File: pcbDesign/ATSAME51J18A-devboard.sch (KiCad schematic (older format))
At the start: 36 parts

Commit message: Finished schematic v0.1
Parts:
- removed C?: 0.47u, Capacitor_SMD:C_0402_1005Metric, symbol Device:C
- removed C? (x2): C, Capacitor_SMD:C_0402_1005Metric, symbol Device:C
- removed C? (x2): 4.7u, Capacitor_SMD:C_0402_1005Metric, symbol Device:C
- removed D?: APA102-2020, LED_SMD:LED-APA102-2020, symbol LED:APA102-2020
- removed D? (x5): D_Schottky, symbol Device:D_Schottky
- removed R?: 10K, Resistor_SMD:R_0402_1005Metric, symbol Device:R
- removed R? (x2): 5.1k, Resistor_SMD:R_0402_1005Metric, symbol Device:R_Small
- removed R?: 0.01, Resistor_SMD:R_0402_1005Metric, symbol Device:R_Small
- removed R? (x2): 10k, Resistor_SMD:R_0402_1005Metric, symbol Device:R_Small
- removed R?: 1k, Resistor_SMD:R_0402_1005Metric, symbol Device:R_Small
- removed R?: 2k, Resistor_SMD:R_0402_1005Metric, symbol Device:R_Small
- removed R?: 1.18k, Resistor_SMD:R_0402_1005Metric, symbol Device:R_Small
- removed R?: 1.13k, Resistor_SMD:R_0402_1005Metric, symbol Device:R_Small
- removed R?: 46.4k, Resistor_SMD:R_0402_1005Metric, symbol Device:R_Small
- removed U?: ATSAME51J18A-A, Package_QFP:TQFP-64_10x10mm_P0.5mm, symbol MCU_Microchip_SAME:ATSAME51J18A-A
- removed U?: LM27762, Package_SON:WSON-12-1EP_3x2mm_P0.5mm_EP1x2.65_ThermalVias, symbol Regulator_SwitchedCapacitor:LM27762
- removed U?: BQ24074RGT, Package_DFN_QFN:VQFN-16-1EP_3x3mm_P0.5mm_EP1.6x1.6mm, symbol Battery_Management:BQ24074RGT
- removed U?: BQ27441DRZR-G1B, Package_SON:Texas_S-PDSO-N12, symbol Battery_Management:BQ27441DRZR-G1B
- removed U?: LM2775QDSGTQ1, DSG0008A, symbol ATSAME51J18A-devboard-rescue:LM2775QDSGTQ1-2021-03-01_13-50-06
- removed U?: SC630AULTRT, SON_ULTRT_SEM, symbol ATSAME51J18A-devboard-rescue:SC630AULTRT-2021-03-02_13-26-31
- removed U?: MIC5219-5.0YMM, Package_SO:MSOP-8_3x3mm_P0.65mm, symbol Regulator_Linear:MIC5219-5.0YMM
- added D?: WS2812B, LED_SMD:LED_WS2812B_PLCC4_5.0x5.0mm_P3.2mm, symbol LED:WS2812B
- added J?: Conn_01x06_Male, symbol Connector:Conn_01x06_Male
- added J?: Conn_01x02_Male, symbol Connector:Conn_01x02_Male
- added J?: Conn_01x01_Male, symbol Connector:Conn_01x01_Male
- added R? (x2): 5.1k, Resistor_SMD:R_0402_1005Metric, symbol Device:R_Small
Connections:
- net labels added: CAN_RX, CAN_S, CAN_TX, NEOPIXEL_DIN, NEOPIXEL_DOUT, QCS, QDAT0, QDAT1, QDAT2, QDAT3, QSCK
- net labels removed: 10[IAT], 11[IPAT][Tx1], 12[IPAT][Rx1], 13[IPAT], 14[IADP], 15[IATP][SDCD], 16[IATP][SDWP], 17[IATP][SDA][QSPID0][SDCMD][I2SMCK], 18[IATP][SCL][QSPID1][SDDAT0][I2SFS], 19[IATP][QSPID2][SDDAT1][I2SSDO], 20[IATP][QSPID3][SDDAT2][I2SSDI], 23[IP][QSPISCK][SDDAT3][I2SSDI], 3[IAD], 4[IPAT][Vref], 5[IAT], 64[IPAT], 6[IAT], 9[IAT], CHARGE_ENABLE, CHARGE_MODE_CH0, CHARGE_MODE_CH1, USB_DETECT, VBUS_BAT_NREG, VBUS_NREG, VBUS_VIN_5V_REG, [SWCLK], [SWDIO]
- wire segments 75 -> 7
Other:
- moved on the sheet: J?, U?

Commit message: Cerrected errors in the schematic and began work on the pcb layout
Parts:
- removed P?: USB_C_Plug, symbol Connector:USB_C_Plug
- removed R?: 5.1k, Resistor_SMD:R_0402_1005Metric, symbol Device:R_Small
- added C1, C2: 100n, Capacitor_SMD:C_0402_1005Metric, symbol Device:C
- added D7: LED, LED_SMD:LED_0402_1005Metric, symbol Device:LED
- added J9: 12401598E4-2A, usb_c:12401598E4-2A, symbol usb_c:12401598E4-2A
- added R1: 5.1k, Resistor_SMD:R_0402_1005Metric, symbol Device:R_Small
- added R19: 10k, Resistor_SMD:R_0402_1005Metric, symbol Device:R_Small
- J1: renamed from J?; footprint (none) -> Connector_Card:microSD_HC_Hirose_DM3D-SF
- J2: renamed from J?; footprint JST_S2B-ZR-SM4A-TF(LF)(SN) -> S2B-ZR-SM4A-TF_LF__SN_:JST_S2B-ZR-SM4A-TF(LF)(SN)
- J3: renamed from J?; footprint JST_SM04B-SRSS-TB(LF)(SN) -> SM04B-SRSS-TB_LF__SN_:JST_SM04B-SRSS-TB(LF)(SN)
- J4, J8: renamed from J?; footprint (none) -> Connector_PinHeader_1.27mm:PinHeader_1x25_P1.27mm_Vertical
- J5: renamed from J?; footprint (none) -> Connector_PinHeader_1.27mm:PinHeader_1x01_P1.27mm_Vertical
- J6: renamed from J?; footprint (none) -> Connector_PinHeader_1.27mm:PinHeader_1x02_P1.27mm_Vertical
- J7: renamed from J?; footprint (none) -> Connector_PinHeader_1.27mm:PinHeader_1x06_P1.27mm_Vertical
- U1: renamed from U?; footprint D8_TEX -> ul_TCAN1051GVDRQ1:TCAN1051GVDRQ1
- gave numbers to parts that had none: 2
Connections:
- net labels added: LED_PIN
- wire segments 7 -> 3
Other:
- moved on the sheet: R2

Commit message: Fixed power rail enabling systems and rearanged pins for easier use
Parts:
- removed J4, J8: Conn_01x25, Connector_PinHeader_1.27mm:PinHeader_1x25_P1.27mm_Vertical, symbol Connector_Generic:Conn_01x25
- added J4: L_PINS, Connector_PinHeader_1.27mm:PinHeader_1x26_P1.27mm_Vertical, symbol Connector_Generic:Conn_01x26
- added J8: R_PINS, Connector_PinHeader_1.27mm:PinHeader_1x26_P1.27mm_Vertical, symbol Connector_Generic:Conn_01x26
- J2: value S2B-ZR-SM4A-TF(LF)(SN) -> BAT
- J3: value SM04B-SRSS-TB(LF)(SN) -> QWIIC
- J5: value Conn_01x01_Male -> NP_OUT
- J6: value Conn_01x02_Male -> USB
- J7: value Conn_01x06_Male -> QSPI
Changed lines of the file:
@@
 P 9300 3150
 F 0 "J3" H 9243 2583 50  0000 C CNN
-F 1 "SM04B-SRSS-TB(LF)(SN)" H 9243 2674 50  0000 C CNN
+F 1 "QWIIC" H 9243 2674 50  0000 C CNN
 F 2 "SM04B-SRSS-TB_LF__SN_:JST_SM04B-SRSS-TB(LF)(SN)" H 9300 3150 50  0001 L BNN
 F 3 "" H 9300 3150 50  0001 L BNN
@@
 P 9300 2350
 F 0 "J2" H 9192 1985 50  0000 C CNN
-F 1 "S2B-ZR-SM4A-TF(LF)(SN)" H 9192 2076 50  0000 C CNN
+F 1 "BAT" H 9192 2076 50  0000 C CNN
 F 2 "S2B-ZR-SM4A-TF_LF__SN_:JST_S2B-ZR-SM4A-TF(LF)(SN)" H 9300 2350 50  0001 L BNN
 F 3 "" H 9300 2350 50  0001 L BNN
@@
 Text GLabel 9250 4400 0    50   BiDi ~ 0
 VBUS_-3V3_CH2_REG
-$Comp
-L Connector_Generic:Conn_01x25 J8
-U 1 1 6061C495
-P 10650 5100
-F 0 "J8" H 10730 5142 50  0000 L CNN
-F 1 "Conn_01x25" H 10730 5051 50  0000 L CNN
-F 2 "Connector_PinHeader_1.27mm:PinHeader_1x25_P1.27mm_Vertical" H 10650 5100 50  0001 C CNN
-F 3 "~" H 10650 5100 50  0001 C CNN
-	1    10650 5100
-	1    0    0    -1
-$EndComp
 Text GLabel 10450 6300 0    50   BiDi ~ 0
 VBUS_-3V3_CH2_REG
@@
 Text GLabel 10450 4000 0    50   BiDi ~ 0
 VBUS_VIN_NREG
-Text GLabel 10450 3900 0    50   BiDi ~ 0
+Text GLabel 10450 3800 0    50   BiDi ~ 0
 VBUS_BAT
 Text GLabel 9250 4100 0    50   BiDi ~ 0
@@
 Text GLabel 10450 4100 0    50   BiDi ~ 0
 AREF
-$Comp
-L Connector_Generic:Conn_01x25 J4
-U 1 1 6045ED31
-P 9450 5100
-F 0 "J4" H 9530 5142 50  0000 L CNN
-F 1 "Conn_01x25" H 9530 5051 50  0000 L CNN
-F 2 "Connector_PinHeader_1.27mm:PinHeader_1x25_P1.27mm_Vertical" H 9450 5100 50  0001 C CNN
-F 3 "~" H 9450 5100 50  0001 C CNN
-	1    9450 5100
-	1    0    0    -1
-$EndComp
 Text GLabel 9250 6000 0    50   BiDi ~ 0
 31[Tx1]
@@
 Text GLabel 9250 4000 0    50   BiDi ~ 0
 RST
-Text GLabel 9250 3900 0    50   BiDi ~ 0
+Text GLabel 9250 3800 0    50   BiDi ~ 0
 EN
 Text GLabel 6550 5000 2    50   BiDi ~ 0
@@
 AR Path="/604C67EC" Ref="J7"  Part="1"
 F 0 "J7" H 10758 3731 50  0000 C CNN
-F 1 "Conn_01x06_Male" H 10758 3640 50  0000 C CNN
+F 1 "QSPI" H 10758 3640 50  0000 C CNN
 F 2 "Connector_PinHeader_1.27mm:PinHeader_1x06_P1.27mm_Vertical" H 10650 3350 50  0001 C CNN
 F 3 "~" H 10650 3350 50  0001 C CNN
@@
 P 10650 2700
 F 0 "J6" H 10758 2881 50  0000 C CNN
-F 1 "Conn_01x02_Male" H 10758 2790 50  0000 C CNN
+F 1 "USB" H 10758 2790 50  0000 C CNN
 F 2 "Connector_PinHeader_1.27mm:PinHeader_1x02_P1.27mm_Vertical" H 10650 2700 50  0001 C CNN
 F 3 "~" H 10650 2700 50  0001 C CNN
@@
 P 10650 2250
 F 0 "J5" H 10758 2431 50  0000 C CNN
-F 1 "Conn_01x01_Male" H 10758 2340 50  0000 C CNN
+F 1 "NP_OUT" H 10758 2340 50  0000 C CNN
 F 2 "Connector_PinHeader_1.27mm:PinHeader_1x01_P1.27mm_Vertical" H 10650 2250 50  0001 C CNN
 F 3 "~" H 10650 2250 50  0001 C CNN
@@
 	0    1    1    0
 $EndComp
+$Comp
+L Connector_Generic:Conn_01x26 J4
+U 1 1 60481B78
+P 9450 5000
+F 0 "J4" H 9530 4992 50  0000 L CNN
+F 1 "L_PINS" H 9530 4901 50  0000 L CNN
+F 2 "Connector_PinHeader_1.27mm:PinHeader_1x26_P1.27mm_Vertical" H 9450 5000 50  0001 C CNN
+F 3 "~" H 9450 5000 50  0001 C CNN
+	1    9450 5000
+	1    0    0    -1
+$EndComp
+$Comp
+L Connector_Generic:Conn_01x26 J8
+U 1 1 60485161
+P 10650 5000
+F 0 "J8" H 10730 4992 50  0000 L CNN
+F 1 "R_PINS" H 10730 4901 50  0000 L CNN
+F 2 "Connector_PinHeader_1.27mm:PinHeader_1x26_P1.27mm_Vertical" H 10650 5000 50  0001 C CNN
+F 3 "~" H 10650 5000 50  0001 C CNN
+	1    10650 5000
+	1    0    0    -1
+$EndComp
+$Comp
+L power:GND #PWR032
+U 1 1 60486DD1
+P 10450 3900
+F 0 "#PWR032" H 10450 3650 50  0001 C CNN
+F 1 "GND" V 10455 3772 50  0000 R CNN
+F 2 "" H 10450 3900 50  0001 C CNN
+F 3 "" H 10450 3900 50  0001 C CNN
+	1    10450 3900
+	0    1    1    0
+$EndComp
+$Comp
+L power:GND #PWR01
+U 1 1 60489437
+P 9250 3900
+F 0 "#PWR01" H 9250 3650 50  0001 C CNN
+F 1 "GND" V 9255 3772 50  0000 R CNN
+F 2 "" H 9250 3900 50  0001 C CNN
+F 3 "" H 9250 3900 50  0001 C CNN
+	1    9250 3900
+	0    1    1    0
+$EndComp

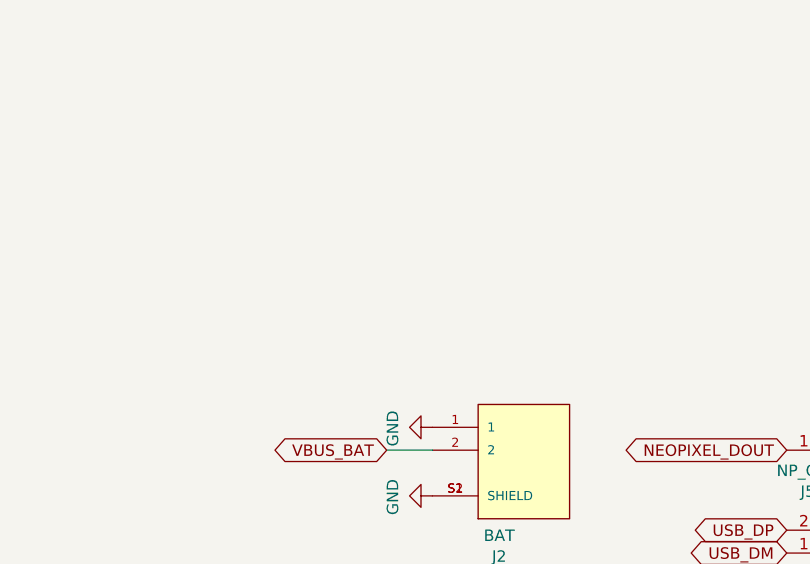
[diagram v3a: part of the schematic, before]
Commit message: Changed pin pitch to 2.54mm
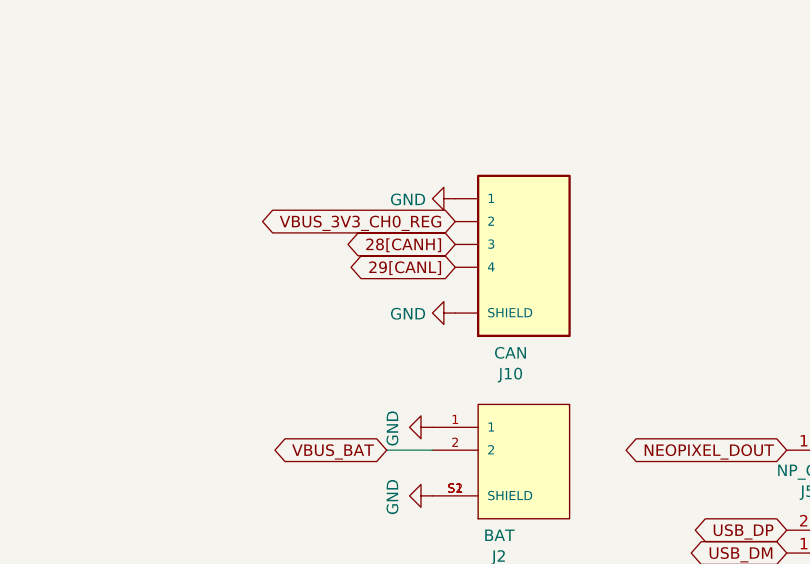
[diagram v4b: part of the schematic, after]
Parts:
- added J10: CAN, SM04B-SRSS-TB_LF__SN_:JST_SM04B-SRSS-TB(LF)(SN), symbol SM04B-SRSS-TB_LF__SN_:SM04B-SRSS-TB(LF)(SN)
- J4, J8: footprint Connector_PinHeader_1.27mm:PinHeader_1x26_P1.27mm_Vertical -> Connector_PinSocket_2.54mm:PinSocket_1x26_P2.54mm_Vertical
- J5: footprint Connector_PinHeader_1.27mm:PinHeader_1x01_P1.27mm_Vertical -> Connector_PinSocket_2.54mm:PinSocket_1x01_P2.54mm_Vertical
- J6: footprint Connector_PinHeader_1.27mm:PinHeader_1x02_P1.27mm_Vertical -> Connector_PinSocket_2.54mm:PinSocket_1x02_P2.54mm_Vertical
- J7: footprint Connector_PinHeader_1.27mm:PinHeader_1x06_P1.27mm_Vertical -> Connector_PinSocket_2.54mm:PinSocket_1x06_P2.54mm_Vertical
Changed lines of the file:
@@
 F 0 "J7" H 10758 3731 50  0000 C CNN
 F 1 "QSPI" H 10758 3640 50  0000 C CNN
-F 2 "Connector_PinHeader_1.27mm:PinHeader_1x06_P1.27mm_Vertical" H 10650 3350 50  0001 C CNN
+F 2 "Connector_PinSocket_2.54mm:PinSocket_1x06_P2.54mm_Vertical" H 10650 3350 50  0001 C CNN
 F 3 "~" H 10650 3350 50  0001 C CNN
 	1    10650 3350
@@
 F 0 "J6" H 10758 2881 50  0000 C CNN
 F 1 "USB" H 10758 2790 50  0000 C CNN
-F 2 "Connector_PinHeader_1.27mm:PinHeader_1x02_P1.27mm_Vertical" H 10650 2700 50  0001 C CNN
+F 2 "Connector_PinSocket_2.54mm:PinSocket_1x02_P2.54mm_Vertical" H 10650 2700 50  0001 C CNN
 F 3 "~" H 10650 2700 50  0001 C CNN
 	1    10650 2700
@@
 F 0 "J5" H 10758 2431 50  0000 C CNN
 F 1 "NP_OUT" H 10758 2340 50  0000 C CNN
-F 2 "Connector_PinHeader_1.27mm:PinHeader_1x01_P1.27mm_Vertical" H 10650 2250 50  0001 C CNN
+F 2 "Connector_PinSocket_2.54mm:PinSocket_1x01_P2.54mm_Vertical" H 10650 2250 50  0001 C CNN
 F 3 "~" H 10650 2250 50  0001 C CNN
 	1    10650 2250
@@
 F 0 "J4" H 9530 4992 50  0000 L CNN
 F 1 "L_PINS" H 9530 4901 50  0000 L CNN
-F 2 "Connector_PinHeader_1.27mm:PinHeader_1x26_P1.27mm_Vertical" H 9450 5000 50  0001 C CNN
+F 2 "Connector_PinSocket_2.54mm:PinSocket_1x26_P2.54mm_Vertical" H 9450 5000 50  0001 C CNN
 F 3 "~" H 9450 5000 50  0001 C CNN
 	1    9450 5000
@@
 F 0 "J8" H 10730 4992 50  0000 L CNN
 F 1 "R_PINS" H 10730 4901 50  0000 L CNN
-F 2 "Connector_PinHeader_1.27mm:PinHeader_1x26_P1.27mm_Vertical" H 10650 5000 50  0001 C CNN
+F 2 "Connector_PinSocket_2.54mm:PinSocket_1x26_P2.54mm_Vertical" H 10650 5000 50  0001 C CNN
 F 3 "~" H 10650 5000 50  0001 C CNN
 	1    10650 5000
@@
 	0    1    1    0
 $EndComp
+$Comp
+L SM04B-SRSS-TB_LF__SN_:SM04B-SRSS-TB(LF)(SN) J10
+U 1 1 604466EE
+P 9300 1350
+F 0 "J10" H 9243 783 50  0000 C CNN
+F 1 "CAN" H 9243 874 50  0000 C CNN
+F 2 "SM04B-SRSS-TB_LF__SN_:JST_SM04B-SRSS-TB(LF)(SN)" H 9300 1350 50  0001 L BNN
+F 3 "" H 9300 1350 50  0001 L BNN
+F 4 "JST" H 9300 1350 50  0001 L BNN "MANUFACTURER"
+F 5 "Manufacturer recommendations" H 9300 1350 50  0001 L BNN "STANDARD"
+	1    9300 1350
+	1    0    0    -1
+$EndComp
+$Comp
+L power:GND #PWR0116
+U 1 1 6044779D
+P 9000 1150
+F 0 "#PWR0116" H 9000 900 50  0001 C CNN
+F 1 "GND" V 9005 1022 50  0000 R CNN
+F 2 "" H 9000 1150 50  0001 C CNN
+F 3 "" H 9000 1150 50  0001 C CNN
+	1    9000 1150
+	0    1    1    0
+$EndComp
+Text GLabel 9000 1250 0    50   BiDi ~ 0
+VBUS_3V3_CH0_REG
+Text GLabel 9000 1350 0    50   BiDi ~ 0
+28[CANH]
+Text GLabel 9000 1450 0    50   BiDi ~ 0
+29[CANL]
+$Comp
+L power:GND #PWR0120
+U 1 1 604483DE
+P 9000 1650
+F 0 "#PWR0120" H 9000 1400 50  0001 C CNN
+F 1 "GND" V 9005 1522 50  0000 R CNN
+F 2 "" H 9000 1650 50  0001 C CNN
+F 3 "" H 9000 1650 50  0001 C CNN
+	1    9000 1650
+	0    1    1    0
+$EndComp

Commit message: Finnished routing
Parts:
- removed J9: 12401598E4-2A, usb_c:12401598E4-2A, symbol usb_c:12401598E4-2A
- added D8: PWR, LED_SMD:LED_0402_1005Metric, symbol Device:LED
- added D9: CHRG, LED_SMD:LED_0402_1005Metric, symbol Device:LED
- added J9: USB4105_REVA, USB4105_REVA:GCT_USB4105_REVA, symbol USB4105_REVA:USB4105_REVA
- added R23, R24: 10k, Resistor_SMD:R_0402_1005Metric, symbol Device:R_Small
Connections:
- net labels added: 30, 31, USB_N, USB_P
- net labels removed: 30[Rx1], 31[Tx1], USB_DM, USB_DP
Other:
- moved on the sheet: R1, R2
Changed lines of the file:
@@
 Comment4 ""
 $EndDescr
-Text GLabel 3800 1850 2    50   BiDi ~ 0
-USB_DP
+Text GLabel 4800 1300 0    50   BiDi ~ 0
+USB_P
 $Comp
 L power:GND #PWR0102
@@
 AREF
 Text GLabel 9250 6000 0    50   BiDi ~ 0
-31[Tx1]
+31
 Text GLabel 9250 5900 0    50   BiDi ~ 0
-30[Rx1]
+30
 Text GLabel 10450 6000 0    50   BiDi ~ 0
 29[CANL]
@@
 $EndComp
 Text GLabel 10450 2700 0    50   BiDi ~ 0
-USB_DM
+USB_N
 Text GLabel 10450 2600 0    50   BiDi ~ 0
-USB_DP
+USB_P
 $Sheet
 S 1950 2550 1150 900
@@
 L Device:R_Small R2
 U 1 1 6060BD83
-P 3900 1950
-F 0 "R2" H 3959 1996 50  0000 L CNN
-F 1 "5.1k" H 3959 1905 50  0000 L CNN
-F 2 "Resistor_SMD:R_0402_1005Metric" H 3900 1950 50  0001 C CNN
-F 3 "~" H 3900 1950 50  0001 C CNN
-	1    3900 1950
+P 6500 1200
+F 0 "R2" H 6559 1246 50  0000 L CNN
+F 1 "5.1k" H 6559 1155 50  0000 L CNN
+F 2 "Resistor_SMD:R_0402_1005Metric" H 6500 1200 50  0001 C CNN
+F 3 "~" H 6500 1200 50  0001 C CNN
+	1    6500 1200
 	0    -1   -1   0
 $EndComp
@@
 LED_PIN
 $Comp
-L Device:LED D7
-U 1 1 60430A33
-P 3150 6600
-F 0 "D7" V 3189 6482 50  0000 R CNN
-F 1 "LED" V 3098 6482 50  0000 R CNN
-F 2 "LED_SMD:LED_0402_1005Metric" H 3150 6600 50  0001 C CNN
-F 3 "~" H 3150 6600 50  0001 C CNN
-	1    3150 6600
-	0    -1   -1   0
-$EndComp
-$Comp
 L power:GND #PWR0101
 U 1 1 604318CC
@@
 	1    0    0    -1
 $EndComp
-$Comp
-L usb_c:12401598E4-2A J9
-U 1 1 604586E0
-P 2200 950
-F 0 "J9" H 3000 1337 60  0000 C CNN
-F 1 "12401598E4-2A" H 3000 1231 60  0000 C CNN
-F 2 "usb_c:12401598E4-2A" H 3000 1190 60  0001 C CNN
-F 3 "" H 2200 950 60  0000 C CNN
-	1    2200 950
-	1    0    0    -1
-$EndComp
-Text GLabel 3800 1550 2    50   BiDi ~ 0
+Text GLabel 6400 1000 2    50   BiDi ~ 0
 VBUS_USB_NREG
 Text GLabel 2200 1750 0    50   BiDi ~ 0
@@
 L power:GND #PWR0103
 U 1 1 6045FB57
-P 4000 1950
-F 0 "#PWR0103" H 4000 1700 50  0001 C CNN
-F 1 "GND" V 4005 1822 50  0000 R CNN
-F 2 "" H 4000 1950 50  0001 C CNN
-F 3 "" H 4000 1950 50  0001 C CNN
-	1    4000 1950
+P 6600 1200
+F 0 "#PWR0103" H 6600 950 50  0001 C CNN
+F 1 "GND" V 6605 1072 50  0000 R CNN
+F 2 "" H 6600 1200 50  0001 C CNN
+F 3 "" H 6600 1200 50  0001 C CNN
+	1    6600 1200
 	0    -1   -1   0
 $EndComp
@@
 L Device:R_Small R1
 U 1 1 60460985
-P 2100 1350
-F 0 "R1" H 2159 1396 50  0000 L CNN
-F 1 "5.1k" H 2159 1305 50  0000 L CNN
-F 2 "Resistor_SMD:R_0402_1005Metric" H 2100 1350 50  0001 C CNN
-F 3 "~" H 2100 1350 50  0001 C CNN
-	1    2100 1350
-	0    1    1    0
+P 4700 1200
+F 0 "R1" H 4759 1246 50  0000 L CNN
+F 1 "5.1k" H 4759 1155 50  0000 L CNN
+F 2 "Resistor_SMD:R_0402_1005Metric" H 4700 1200 50  0001 C CNN
+F 3 "~" H 4700 1200 50  0001 C CNN
+	1    4700 1200
+	0    -1   -1   0
 $EndComp
 $Comp
 L power:GND #PWR0105
 U 1 1 604625F2
-P 2000 1350
-F 0 "#PWR0105" H 2000 1100 50  0001 C CNN
-F 1 "GND" V 2005 1222 50  0000 R CNN
-F 2 "" H 2000 1350 50  0001 C CNN
-F 3 "" H 2000 1350 50  0001 C CNN
-	1    2000 1350
-	0    1    1    0
-$EndComp
-Text GLabel 2200 1450 0    50   BiDi ~ 0
-USB_DP
-Text GLabel 3800 1750 2    50   BiDi ~ 0
-USB_DM
-Text GLabel 2200 1550 0    50   BiDi ~ 0
-USB_DM
+P 4600 1200
+F 0 "#PWR0105" H 4600 950 50  0001 C CNN
+F 1 "GND" V 4605 1072 50  0000 R CNN
+F 2 "" H 4600 1200 50  0001 C CNN
+F 3 "" H 4600 1200 50  0001 C CNN
+	1    4600 1200
+	0    1    1    0
+$EndComp
+Text GLabel 6400 1300 2    50   BiDi ~ 0
+USB_P
+Text GLabel 4800 1400 0    50   BiDi ~ 0
+USB_N
+Text GLabel 6400 1400 2    50   BiDi ~ 0
+USB_N
 $Comp
 L power:GND #PWR0106
 U 1 1 60463C59
-P 3800 1250
-F 0 "#PWR0106" H 3800 1000 50  0001 C CNN
-F 1 "GND" V 3805 1122 50  0000 R CNN
-F 2 "" H 3800 1250 50  0001 C CNN
-F 3 "" H 3800 1250 50  0001 C CNN
-	1    3800 1250
+P 6400 1700
+F 0 "#PWR0106" H 6400 1450 50  0001 C CNN
+F 1 "GND" V 6405 1572 50  0000 R CNN
+F 2 "" H 6400 1700 50  0001 C CNN
+F 3 "" H 6400 1700 50  0001 C CNN
+	1    6400 1700
 	0    -1   -1   0
 $EndComp
@@
 	0    1    1    0
 $EndComp
+$Comp
+L power:GND #PWR0121
+U 1 1 60450E98
+P 2750 6750
+F 0 "#PWR0121" H 2750 6500 50  0001 C CNN
+F 1 "GND" H 2755 6577 50  0000 C CNN
+F 2 "" H 2750 6750 50  0001 C CNN
+F 3 "" H 2750 6750 50  0001 C CNN
+	1    2750 6750
+	1    0    0    -1
+$EndComp
+$Comp
+L Device:R_Small R23
+U 1 1 60451248
+P 2750 6350
+F 0 "R23" H 2809 6396 50  0000 L CNN
+F 1 "10k" H 2809 6305 50  0000 L CNN
+F 2 "Resistor_SMD:R_0402_1005Metric" H 2750 6350 50  0001 C CNN
+F 3 "~" H 2750 6350 50  0001 C CNN
+	1    2750 6350
+	1    0    0    -1
+$EndComp
+Text GLabel 2750 6250 1    50   BiDi ~ 0
+VBUS_3V3_CH0_REG
+$Comp
+L Device:R_Small R24
+U 1 1 604A943E
+P 3600 6350
+F 0 "R24" H 3659 6396 50  0000 L CNN
+F 1 "10k" H 3659 6305 50  0000 L CNN
+F 2 "Resistor_SMD:R_0402_1005Metric" H 3600 6350 50  0001 C CNN
+F 3 "~" H 3600 6350 50  0001 C CNN
+	1    3600 6350
+	1    0    0    -1
+$EndComp
+Text GLabel 3600 6250 1    50   BiDi ~ 0
+VBUS_3V3_CH0_REG
+Text GLabel 3600 6750 3    50   BiDi ~ 0
+CHRG
+$Comp
+L Device:LED D9
+U 1 1 604A8FE1
+P 3600 6600
+F 0 "D9" V 3639 6482 50  0000 R CNN
+F 1 "CHRG" V 3548 6482 50  0000 R CNN
+F 2 "LED_SMD:LED_0402_1005Metric" H 3600 6600 50  0001 C CNN
+F 3 "~" H 3600 6600 50  0001 C CNN
+	1    3600 6600
+	0    -1   -1   0
+$EndComp
+$Comp
+L Device:LED D7
+U 1 1 60430A33
+P 3150 6600
+F 0 "D7" V 3189 6482 50  0000 R CNN
+F 1 "LED" V 3098 6482 50  0000 R CNN
+F 2 "LED_SMD:LED_0402_1005Metric" H 3150 6600 50  0001 C CNN
+F 3 "~" H 3150 6600 50  0001 C CNN
+	1    3150 6600
+	0    -1   -1   0
+$EndComp
+$Comp
+L Device:LED D8
+U 1 1 60450004
+P 2750 6600
+F 0 "D8" V 2789 6482 50  0000 R CNN
+F 1 "PWR" V 2698 6482 50  0000 R CNN
+F 2 "LED_SMD:LED_0402_1005Metric" H 2750 6600 50  0001 C CNN
+F 3 "~" H 2750 6600 50  0001 C CNN
+	1    2750 6600
+	0    -1   -1   0
+$EndComp
+$Comp
+L USB4105_REVA:USB4105_REVA J9
+U 1 1 60574706
+P 5600 1400
+F 0 "J9" H 5600 2067 50  0000 C CNN
+F 1 "USB4105_REVA" H 5600 1976 50  0000 C CNN
+F 2 "USB4105_REVA:GCT_USB4105_REVA" H 5600 1400 50  0001 L BNN
+F 3 "" H 5600 1400 50  0001 L BNN
+F 4 "3.31 mm" H 5600 1400 50  0001 L BNN "MAXIMUM_PACKAGE_HEIGHT"
+F 5 "GCT" H 5600 1400 50  0001 L BNN "MANUFACTURER"
+F 6 "0.2" H 5600 1400 50  0001 L BNN "PARTREV"
+F 7 "Manufacturer Recommendations" H 5600 1400 50  0001 L BNN "STANDARD"
+	1    5600 1400
+	1    0    0    -1
+$EndComp
 $EndSCHEMATC
